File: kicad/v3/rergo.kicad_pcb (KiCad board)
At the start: 2 copper layers, 132.6 x 94.1 mm, 22 parts

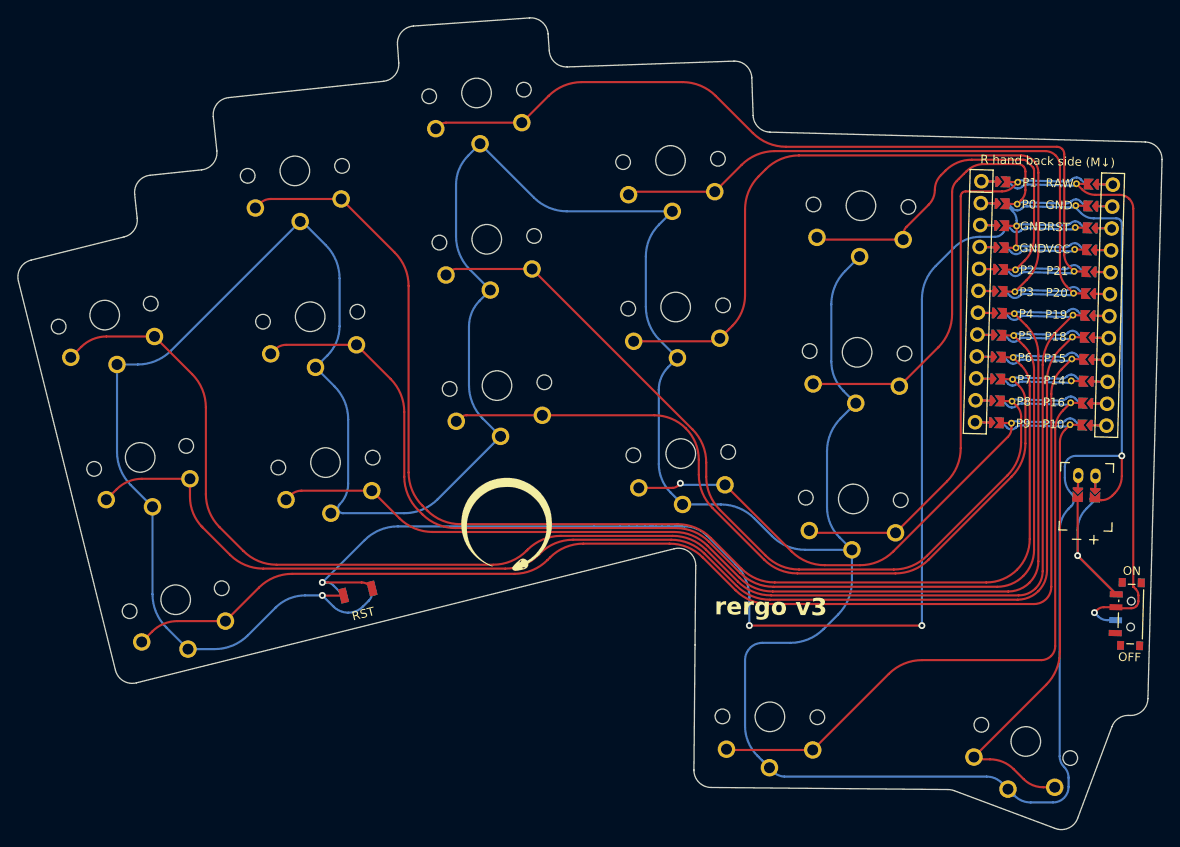
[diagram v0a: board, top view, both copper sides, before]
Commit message: updated v3 no round tracks + added gerber files
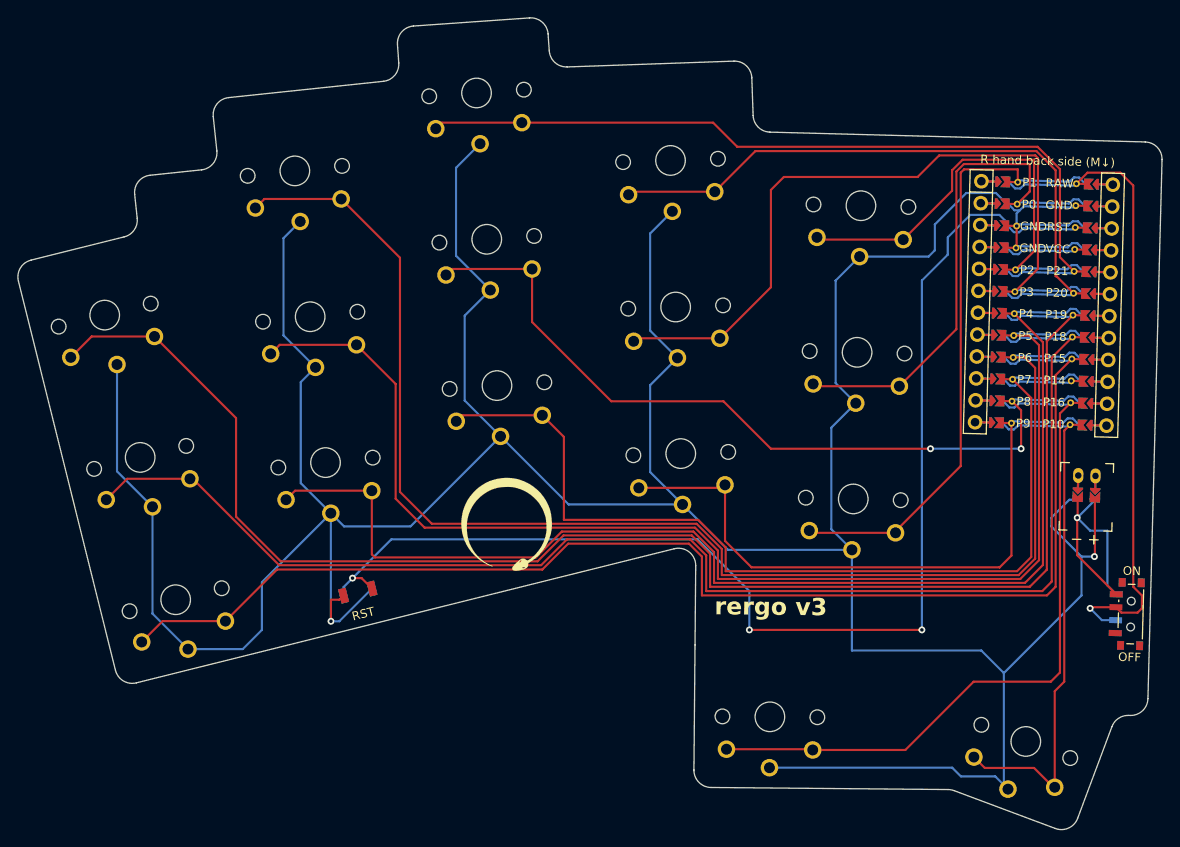
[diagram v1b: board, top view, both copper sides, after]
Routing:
- net GND: track 504.2 -> 476.2 mm
- net P9: track 63.9 -> 76.9 mm, vias 1 -> 0
- net P7: track 101.0 -> 113.7 mm
- net P8: track 105.9 -> 95.0 mm, vias 0 -> 2
- net P4: track 132.9 -> 142.7 mm
- net P5: track 143.9 -> 149.5 mm
- net P6: track 156.7 -> 162.3 mm
- net RAW: track 71.9 -> 77.0 mm
- net RST: track 150.3 -> 145.2 mm
- net P21: track 101.5 -> 97.2 mm
- net P1: track 69.0 -> 73.1 mm
- net P15: track 149.5 -> 153.2 mm
- net P0: track 59.2 -> 61.7 mm
- net P16: track 81.6 -> 84.0 mm
- net P19: track 177.5 -> 179.0 mm
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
